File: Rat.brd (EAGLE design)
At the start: 52.1 x 45.7 mm, 37 parts, among them IC1 LM308N, Q1A 2N5458, Q1B MMBF5458

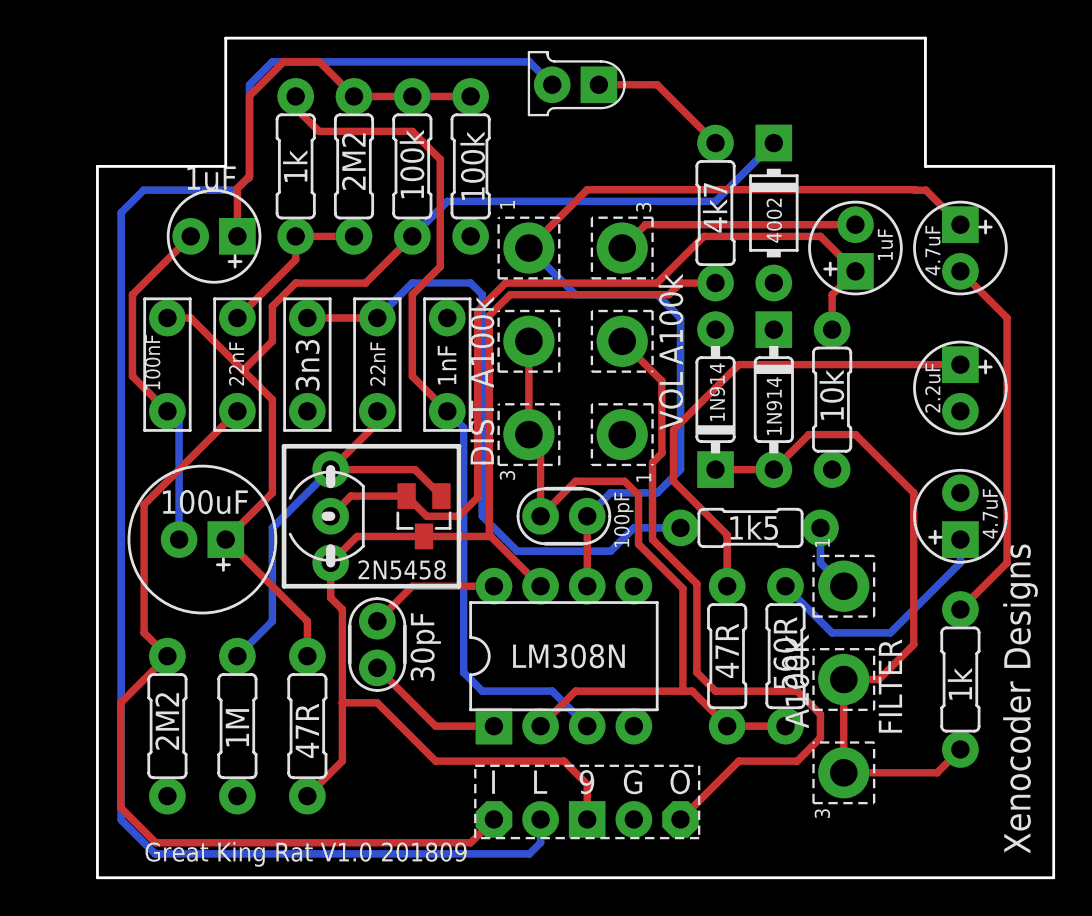
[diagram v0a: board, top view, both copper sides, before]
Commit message: Updated SOT23 footprint to right connections
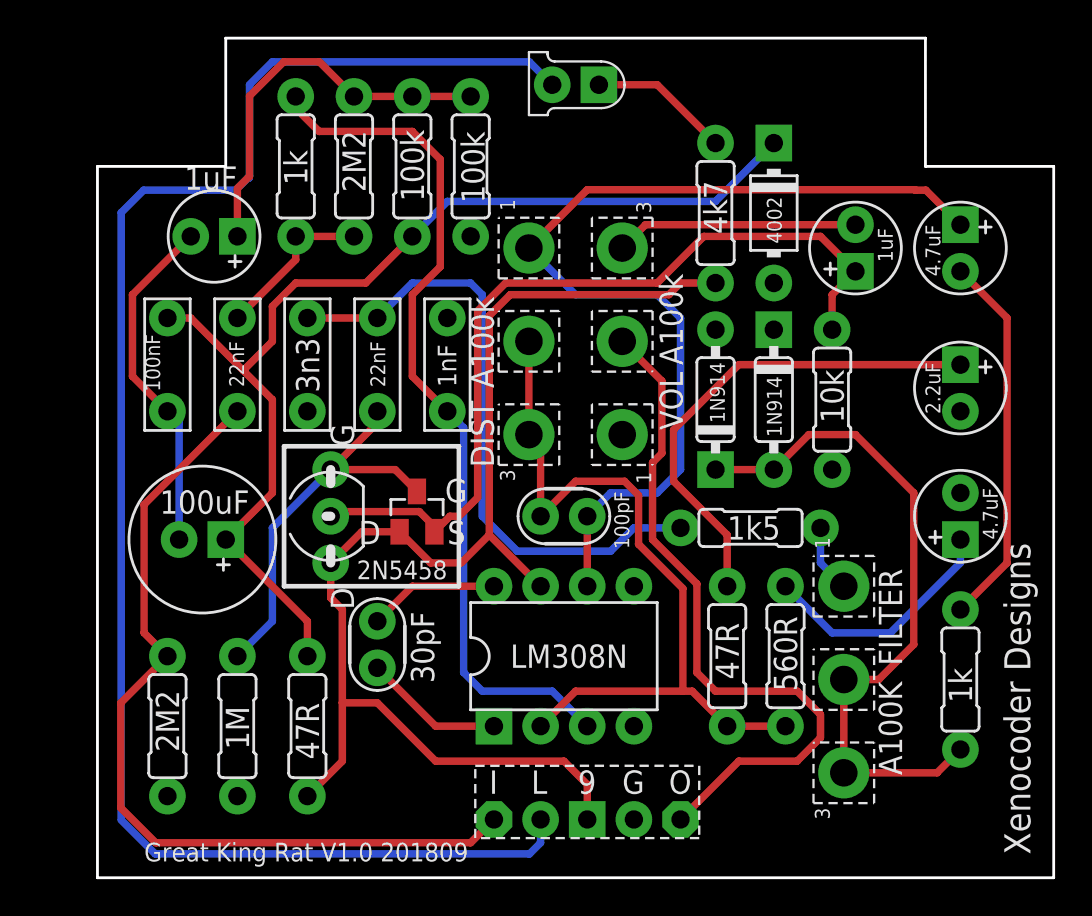
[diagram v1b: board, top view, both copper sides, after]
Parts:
- moved Q1B 0.46 mm to (17.4, 19.9), turned to 0 degrees
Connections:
- net +9V: now also Q1B.1; no longer Q1B.3
- net N$13: now also Q1B.3; no longer Q1B.1
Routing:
- net N$13: track 23.1 -> 21.7 mm
- net +9V: track 69.1 -> 70.4 mm
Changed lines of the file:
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@@
 <?xml version="1.0" encoding="utf-8"?>
 <!DOCTYPE eagle SYSTEM "eagle.dtd">
-<eagle version="9.1.3">
+<eagle version="9.2.2">
 <drawing>
 <settings>
@@
 </element>
 <element name="FILTER" library="mb_pots" package="16MM" value="A100K" x="40.64" y="10.795" smashed="yes" rot="R90">
-<attribute name="NAME" x="43.815" y="7.747" size="1.27" layer="21" ratio="12" rot="R90"/>
-<attribute name="VALUE" x="38.735" y="8.128" size="1.27" layer="25" ratio="12" rot="R90"/>
+<attribute name="NAME" x="43.815" y="11.557" size="1.27" layer="21" ratio="12" rot="R90"/>
+<attribute name="VALUE" x="43.815" y="5.588" size="1.27" layer="25" ratio="12" rot="R90"/>
 </element>
 <element name="IC1" library="mb_ics" package="DIL08" value="LM308N" x="25.4" y="12.065" smashed="yes">
@@
 <attribute name="VALUE" x="19.05" y="17.272" size="1.016" layer="25" ratio="12" rot="R180"/>
 </element>
-<element name="Q1B" library="xc_library" package="SOT23" value="MMBF5458" x="17.78" y="19.685" smashed="yes" rot="R180"/>
+<element name="Q1B" library="xc_library" package="SOT23" value="MMBF5458" x="17.399" y="19.939" smashed="yes"/>
 <element name="R1" library="mb_resistors" package="R0207/3" value="2M2" x="3.81" y="8.255" smashed="yes" rot="R90">
 <attribute name="VALUE" x="4.445" y="6.858" size="1.27" layer="25" font="vector" ratio="12" rot="R90"/>
@@
 <signal name="+9V">
 <contactref element="IC1" pad="7"/>
-<contactref element="Q1B" pad="3"/>
+<contactref element="Q1B" pad="1"/>
 <contactref element="Q1A" pad="3"/>
 <contactref element="R10" pad="2"/>
 <contactref element="R12" pad="1"/>
-<wire x1="12.7" y1="17.145" x2="14.14" y2="18.585" width="0.4064" layer="1"/>
-<wire x1="14.14" y1="18.585" x2="17.78" y2="18.585" width="0.4064" layer="1"/>
 <contactref element="U$1" pad="3"/>
-<wire x1="24.13" y1="15.875" x2="21.42" y2="18.585" width="0.4064" layer="1"/>
-<wire x1="21.42" y1="18.585" x2="17.78" y2="18.585" width="0.4064" layer="1"/>
+<wire x1="24.13" y1="15.875" x2="21.336" y2="18.669" width="0.4064" layer="1"/>
 <wire x1="12.7" y1="17.145" x2="12.7" y2="15.24" width="0.4064" layer="1"/>
 <wire x1="12.7" y1="15.24" x2="13.335" y2="14.605" width="0.4064" layer="1"/>
@@
 <wire x1="22.479" y1="31.75" x2="21.336" y2="30.607" width="0.4064" layer="1"/>
 <wire x1="21.336" y1="30.607" x2="21.336" y2="18.669" width="0.4064" layer="1"/>
-<wire x1="21.336" y1="18.669" x2="21.42" y2="18.585" width="0.4064" layer="1"/>
 <wire x1="31.115" y1="31.75" x2="22.479" y2="31.75" width="0.4064" layer="1"/>
+<wire x1="16.449" y1="18.839" x2="14.394" y2="18.839" width="0.4064" layer="1"/>
+<wire x1="14.394" y1="18.839" x2="12.7" y2="17.145" width="0.4064" layer="1"/>
+<wire x1="16.449" y1="18.839" x2="18.143" y2="17.145" width="0.4064" layer="1"/>
+<wire x1="19.812" y1="17.145" x2="21.336" y2="18.669" width="0.4064" layer="1"/>
+<wire x1="18.143" y1="17.145" x2="19.812" y2="17.145" width="0.4064" layer="1"/>
 </signal>
 <signal name="N$4">
@@
 <contactref element="C9" pad="2"/>
 <contactref element="Q1A" pad="1"/>
-<contactref element="Q1B" pad="1"/>
+<contactref element="Q1B" pad="3"/>
 <wire x1="7.62" y1="12.065" x2="9.525" y2="13.97" width="0.4064" layer="16"/>
 <wire x1="9.525" y1="19.05" x2="12.7" y2="22.225" width="0.4064" layer="16"/>
@@
 <wire x1="12.7" y1="22.225" x2="15.24" y2="24.765" width="0.4064" layer="1"/>
 <wire x1="15.24" y1="24.765" x2="15.24" y2="25.4" width="0.4064" layer="1"/>
-<wire x1="18.73" y1="20.785" x2="17.29" y2="22.225" width="0.4064" layer="1"/>
-<wire x1="17.29" y1="22.225" x2="12.7" y2="22.225" width="0.4064" layer="1"/>
+<wire x1="17.399" y1="21.039" x2="16.213" y2="22.225" width="0.4064" layer="1"/>
+<wire x1="16.213" y1="22.225" x2="12.7" y2="22.225" width="0.4064" layer="1"/>
 </signal>
 <signal name="N$15">
@@
 <contactref element="C10" pad="+"/>
 <contactref element="R9" pad="2"/>
-<wire x1="12.7" y1="19.685" x2="13.8" y2="20.785" width="0.4064" layer="1"/>
-<wire x1="13.8" y1="20.785" x2="16.83" y2="20.785" width="0.4064" layer="1"/>
-<wire x1="16.83" y1="20.785" x2="17.93" y2="19.685" width="0.4064" layer="1"/>
-<wire x1="17.93" y1="19.685" x2="19.685" y2="19.685" width="0.4064" layer="1"/>
 <wire x1="22.225" y1="32.385" x2="20.701" y2="30.861" width="0.4064" layer="1"/>
 <wire x1="39.37" y1="34.925" x2="41.275" y2="33.02" width="0.4064" layer="1"/>
-<wire x1="20.701" y1="20.701" x2="19.685" y2="19.685" width="0.4064" layer="1"/>
+<wire x1="19.685" y1="19.685" x2="20.701" y2="20.701" width="0.4064" layer="1"/>
 <wire x1="22.225" y1="32.385" x2="30.48" y2="32.385" width="0.4064" layer="1"/>
 <wire x1="30.48" y1="32.385" x2="33.02" y2="34.925" width="0.4064" layer="1"/>
@@
 <wire x1="40.005" y1="31.75" x2="41.275" y2="33.02" width="0.4064" layer="1"/>
 <wire x1="20.701" y1="30.861" x2="20.701" y2="20.701" width="0.4064" layer="1"/>
+<wire x1="18.349" y1="18.839" x2="18.4875" y2="18.9775" width="0.4064" layer="1"/>
+<wire x1="18.4875" y1="18.9775" x2="19.195" y2="19.685" width="0.4064" layer="1"/>
+<wire x1="19.195" y1="19.685" x2="19.685" y2="19.685" width="0.4064" layer="1"/>
+<wire x1="12.7" y1="19.685" x2="12.954" y2="19.939" width="0.4064" layer="1"/>
+<wire x1="12.954" y1="19.939" x2="17.526" y2="19.939" width="0.4064" layer="1"/>
+<wire x1="17.526" y1="19.939" x2="18.4875" y2="18.9775" width="0.4064" layer="1"/>
 </signal>
 <signal name="N$14">

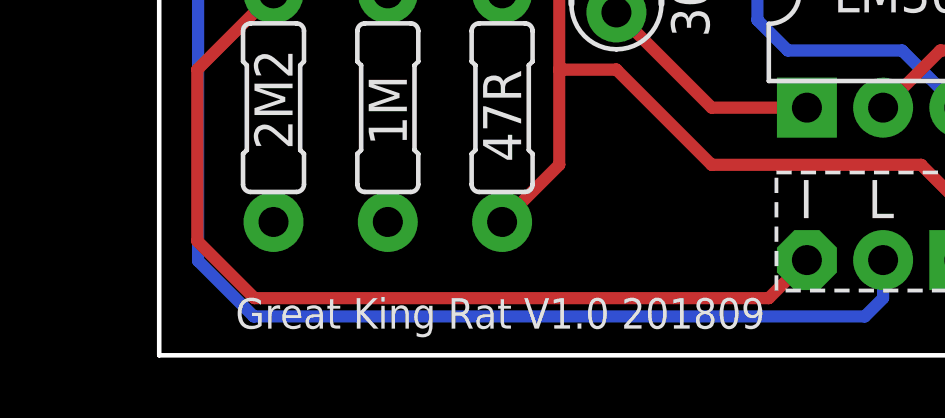
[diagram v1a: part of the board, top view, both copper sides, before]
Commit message: Fixed issue of SMD 5458
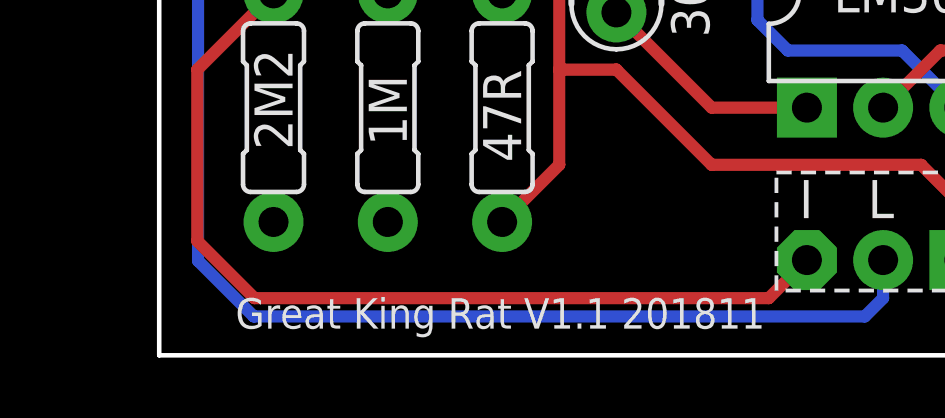
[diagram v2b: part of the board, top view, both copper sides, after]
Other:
- board text added: "Great King Rat V1.1 201811"
- board text removed: "Great King Rat V1.0 201809"
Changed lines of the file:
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@@
 <wire x1="10.16" y1="15.875" x2="10.16" y2="23.495" width="0.254" layer="25"/>
 <text x="50.8" y="1.27" size="1.4224" layer="25" font="vector" rot="R90">Xenocoder Designs</text>
-<text x="20.193" y="1.905" size="1.016" layer="25" font="vector" rot="R180">Great King Rat V1.0 201809</text>
+<text x="20.193" y="1.905" size="1.016" layer="25" font="vector" rot="R180">Great King Rat V1.1 201811</text>
 </plain>
 <attributes>

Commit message: Files for Seeed Studio
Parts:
- added SW-IN: (no value), mb_supply:SQUARE
- added SW-OUT: (no value), mb_supply:ROUND
- D1: value 1N914 -> CLIP-D1
- D2: value 1N914 -> CLIP-D2
- moved R6 20.3 mm to (33.7, 26.0)
- moved R9 17.9 mm to (47.0, 9.53)
- moved D2 3.18 mm to (40.0, 26.0)
- moved D1 3.17 mm to (36.8, 26.0)
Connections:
- net GND: now also SW-OUT.1
- net N$11: now also SW-IN.1
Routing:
- net N$15: track 46.3 -> 69.8 mm
- net N$11: track 37.7 -> 28.4 mm
- net N$10: track 20.5 -> 17.7 mm
- net N$4: track 26.8 -> 26.1 mm
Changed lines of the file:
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@@
 <attribute name="VALUE" x="14.859" y="29.21" size="0.8128" layer="25" ratio="12" rot="R270"/>
 </element>
-<element name="D1" library="mb_diodes" package="DO35-3" value="1N914" x="33.655" y="26.035" smashed="yes" rot="R90">
-<attribute name="VALUE" x="34.163" y="24.765" size="0.8128" layer="25" ratio="12" rot="R90"/>
-</element>
-<element name="D2" library="mb_diodes" package="DO35-3" value="1N914" x="36.83" y="26.035" smashed="yes" rot="R270">
-<attribute name="VALUE" x="36.449" y="27.305" size="0.8128" layer="25" ratio="12" rot="R270"/>
+<element name="D1" library="mb_diodes" package="DO35-3" value="CLIP-D1" x="36.83" y="26.035" smashed="yes" rot="R90">
+<attribute name="VALUE" x="37.211" y="24.765" size="0.6096" layer="25" ratio="12" rot="R90"/>
+</element>
+<element name="D2" library="mb_diodes" package="DO35-3" value="CLIP-D2" x="40.005" y="26.035" smashed="yes" rot="R270">
+<attribute name="VALUE" x="39.624" y="27.178" size="0.6096" layer="25" ratio="12" rot="R270"/>
 </element>
 <element name="D3" library="mb_diodes" package="DO41-3" value="4002" x="36.83" y="36.195" smashed="yes" rot="R270">
@@
 <attribute name="VALUE" x="38.1" y="10.16" size="1.27" layer="25" font="vector" ratio="12" rot="R90"/>
 </element>
-<element name="R6" library="mb_resistors" package="R0207/3" value="1k" x="46.99" y="10.795" smashed="yes" rot="R90">
-<attribute name="VALUE" x="47.625" y="9.525" size="1.27" layer="25" font="vector" ratio="12" rot="R90"/>
+<element name="R6" library="mb_resistors" package="R0207/3" value="1k" x="33.655" y="26.035" smashed="yes" rot="R90">
+<attribute name="VALUE" x="34.29" y="24.765" size="1.27" layer="25" font="vector" ratio="12" rot="R90"/>
 </element>
 <element name="R7" library="mb_resistors" package="R0207/3" value="1k5" x="35.56" y="19.05" smashed="yes">
@@
 <attribute name="VALUE" x="8.255" y="6.985" size="1.27" layer="25" font="vector" ratio="12" rot="R90"/>
 </element>
-<element name="R9" library="mb_resistors" package="R0207/3" value="10k" x="40.005" y="26.035" smashed="yes" rot="R90">
-<attribute name="VALUE" x="40.64" y="24.765" size="1.27" layer="25" font="vector" ratio="12" rot="R90"/>
+<element name="R9" library="mb_resistors" package="R0207/3" value="10k" x="46.99" y="9.525" smashed="yes" rot="R90">
+<attribute name="VALUE" x="47.625" y="8.255" size="1.27" layer="25" font="vector" ratio="12" rot="R90"/>
 </element>
 <element name="VOL" library="mb_pots" package="16MM" value="A100k" x="28.575" y="29.21" smashed="yes" rot="R270">
@@
 </element>
 <element name="U$1" library="xc_library" package="BOARDLINK" value="BOARDLINK" x="24.13" y="3.175" smashed="yes"/>
+<element name="SW-IN" library="mb_supply" package="SQUARE" value="" x="43.18" y="22.225" smashed="yes">
+<attribute name="NAME" x="44.45" y="22.352" size="0.8128" layer="25" ratio="12"/>
+</element>
+<element name="SW-OUT" library="mb_supply" package="ROUND" value="" x="43.18" y="29.845" smashed="yes">
+<attribute name="NAME" x="44.45" y="29.591" size="0.8128" layer="25" ratio="12"/>
+</element>
 </elements>
 <signals>
@@
 <vertex x="0" y="38.735"/>
 </polygon>
+<contactref element="SW-OUT" pad="1"/>
 </signal>
 <signal name="N$1">
@@
 <wire x1="34.29" y1="15.875" x2="34.29" y2="18.669" width="0.4064" layer="1"/>
 <wire x1="34.29" y1="18.669" x2="31.369" y2="21.59" width="0.4064" layer="1"/>
-<wire x1="31.369" y1="21.59" x2="31.369" y2="24.384" width="0.4064" layer="1"/>
-<wire x1="34.925" y1="27.94" x2="46.99" y2="27.94" width="0.4064" layer="1"/>
-<wire x1="31.369" y1="24.384" x2="34.925" y2="27.94" width="0.4064" layer="1"/>
+<wire x1="31.369" y1="21.59" x2="31.369" y2="23.114" width="0.4064" layer="1"/>
+<wire x1="43.815" y1="24.765" x2="46.99" y2="27.94" width="0.4064" layer="1"/>
+<wire x1="43.815" y1="24.765" x2="33.02" y2="24.765" width="0.4064" layer="1"/>
+<wire x1="31.369" y1="23.114" x2="33.02" y2="24.765" width="0.4064" layer="1"/>
 </signal>
 <signal name="N$5">
 <contactref element="R5" pad="2"/>
 <contactref element="C6" pad="+"/>
-<wire x1="37.465" y1="15.875" x2="40.005" y2="13.335" width="0.4064" layer="16"/>
+<wire x1="40.005" y1="13.335" x2="37.465" y2="15.875" width="0.4064" layer="16"/>
 <wire x1="46.99" y1="17.145" x2="46.99" y2="18.415" width="0.4064" layer="16"/>
-<wire x1="40.005" y1="13.335" x2="43.18" y2="13.335" width="0.4064" layer="16"/>
+<wire x1="43.18" y1="13.335" x2="40.005" y2="13.335" width="0.4064" layer="16"/>
 <wire x1="43.18" y1="13.335" x2="46.99" y2="17.145" width="0.4064" layer="16"/>
 </signal>
@@
 <contactref element="R6" pad="2"/>
 <contactref element="C7" pad="-"/>
-<wire x1="46.99" y1="33.02" x2="49.53" y2="30.48" width="0.4064" layer="1"/>
-<wire x1="49.53" y1="17.145" x2="46.99" y2="14.605" width="0.4064" layer="1"/>
-<wire x1="49.53" y1="30.48" x2="49.53" y2="17.145" width="0.4064" layer="1"/>
+<wire x1="33.655" y1="29.845" x2="33.655" y2="29.21" width="0.4064" layer="1"/>
+<wire x1="33.655" y1="29.21" x2="34.925" y2="27.94" width="0.4064" layer="1"/>
+<wire x1="34.925" y1="27.94" x2="43.815" y2="27.94" width="0.4064" layer="1"/>
+<wire x1="43.815" y1="27.94" x2="46.99" y2="31.115" width="0.4064" layer="1"/>
+<wire x1="46.99" y1="31.115" x2="46.99" y2="33.02" width="0.4064" layer="1"/>
 </signal>
 <signal name="N$11">
@@
 <contactref element="FILTER" pad="3"/>
 <contactref element="FILTER" pad="2"/>
+<wire x1="40.64" y1="5.715" x2="40.64" y2="10.795" width="0.4064" layer="1"/>
+<contactref element="SW-IN" pad="1"/>
 <wire x1="33.655" y1="22.225" x2="36.83" y2="22.225" width="0.4064" layer="1"/>
-<wire x1="36.83" y1="22.225" x2="38.735" y2="24.13" width="0.4064" layer="1"/>
-<wire x1="38.735" y1="24.13" x2="41.275" y2="24.13" width="0.4064" layer="1"/>
-<wire x1="41.275" y1="24.13" x2="44.45" y2="20.955" width="0.4064" layer="1"/>
-<wire x1="44.45" y1="12.7" x2="44.45" y2="20.955" width="0.4064" layer="1"/>
-<wire x1="40.64" y1="5.715" x2="45.72" y2="5.715" width="0.4064" layer="1"/>
-<wire x1="45.72" y1="5.715" x2="46.99" y2="6.985" width="0.4064" layer="1"/>
-<wire x1="40.64" y1="10.795" x2="42.545" y2="10.795" width="0.4064" layer="1"/>
-<wire x1="42.545" y1="10.795" x2="44.45" y2="12.7" width="0.4064" layer="1"/>
-<wire x1="40.64" y1="5.715" x2="40.64" y2="10.795" width="0.4064" layer="1"/>
+<wire x1="40.005" y1="22.225" x2="36.83" y2="22.225" width="0.4064" layer="1"/>
+<wire x1="43.18" y1="22.225" x2="40.005" y2="22.225" width="0.4064" layer="1"/>
+<wire x1="40.005" y1="22.225" x2="43.18" y2="19.05" width="0.4064" layer="1"/>
+<wire x1="43.18" y1="19.05" x2="43.18" y2="13.97" width="0.4064" layer="1"/>
+<wire x1="43.18" y1="13.97" x2="40.64" y2="11.43" width="0.4064" layer="1"/>
+<wire x1="40.64" y1="11.43" x2="40.64" y2="10.795" width="0.4064" layer="1"/>
 </signal>
 <signal name="N$12">
@@
 <wire x1="39.37" y1="34.925" x2="41.275" y2="33.02" width="0.4064" layer="1"/>
 <wire x1="19.685" y1="19.685" x2="20.701" y2="20.701" width="0.4064" layer="1"/>
-<wire x1="22.225" y1="32.385" x2="30.48" y2="32.385" width="0.4064" layer="1"/>
+<wire x1="30.48" y1="32.385" x2="22.225" y2="32.385" width="0.4064" layer="1"/>
 <wire x1="30.48" y1="32.385" x2="33.02" y2="34.925" width="0.4064" layer="1"/>
 <wire x1="33.02" y1="34.925" x2="39.37" y2="34.925" width="0.4064" layer="1"/>
-<wire x1="40.005" y1="29.845" x2="40.005" y2="31.75" width="0.4064" layer="1"/>
-<wire x1="40.005" y1="31.75" x2="41.275" y2="33.02" width="0.4064" layer="1"/>
 <wire x1="20.701" y1="30.861" x2="20.701" y2="20.701" width="0.4064" layer="1"/>
 <wire x1="18.349" y1="18.839" x2="18.4875" y2="18.9775" width="0.4064" layer="1"/>
@@
 <wire x1="12.954" y1="19.939" x2="17.526" y2="19.939" width="0.4064" layer="1"/>
 <wire x1="17.526" y1="19.939" x2="18.4875" y2="18.9775" width="0.4064" layer="1"/>
+<wire x1="45.085" y1="31.115" x2="43.18" y2="33.02" width="0.4064" layer="16"/>
+<wire x1="41.275" y1="33.02" x2="43.18" y2="33.02" width="0.4064" layer="16"/>
+<wire x1="48.26" y1="31.115" x2="49.53" y2="29.845" width="0.4064" layer="16"/>
+<wire x1="49.53" y1="29.845" x2="49.53" y2="15.875" width="0.4064" layer="16"/>
+<wire x1="49.53" y1="15.875" x2="46.99" y2="13.335" width="0.4064" layer="16"/>
+<wire x1="45.085" y1="31.115" x2="48.26" y2="31.115" width="0.4064" layer="16"/>
 </signal>
 <signal name="N$14">
